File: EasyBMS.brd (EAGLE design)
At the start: 100 x 100 mm, 147 parts, among them Q1 BSS84LT1G, Q10 BSS84LT1G, Q11 BSS84LT1G, Q12 BSS84LT1G, Q14 BSS84LT1G, Q3 BSS84LT1G, Q4 BSS84LT1G, Q5 BSS84LT1G, Q6 BSS84LT1G, Q7 BSS84LT1G, Q8 BSS84LT1G, Q9 BSS84LT1G

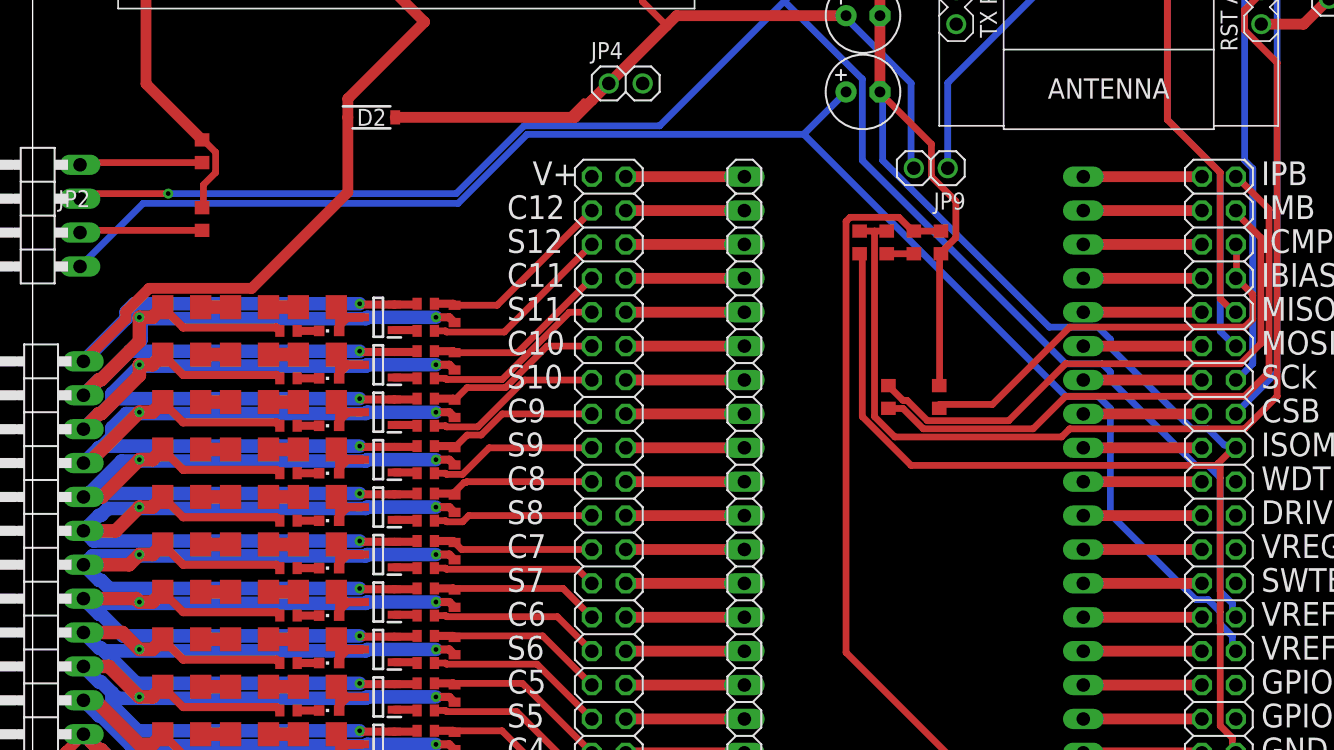
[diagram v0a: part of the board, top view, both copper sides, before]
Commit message: supply voltage bug removed
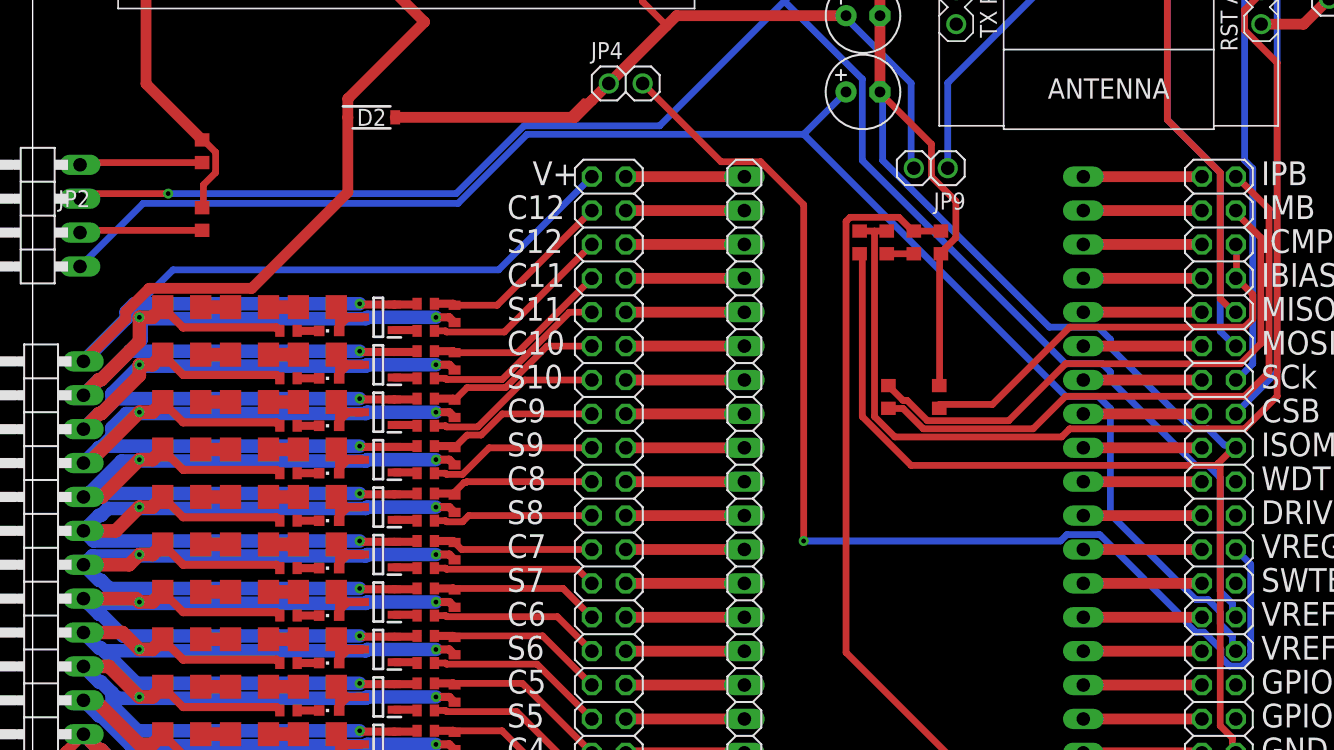
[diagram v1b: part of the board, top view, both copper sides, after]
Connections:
- removed net N$106: JP4.2
- removed net V+: JP5.1
- net P13: now also JP5.1
- net VREG: now also JP4.2
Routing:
- net VREG: track 0.00 -> 88.1 mm, vias 0 -> 1
- net P13: track 122.6 -> 166.5 mm
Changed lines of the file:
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@@
 <wire x1="89.916" y1="28.0416" x2="90.17" y2="27.94" width="0.508" layer="16"/>
-</signal>
-<signal name="N$106">
-<contactref element="JP4" pad="2"/>
 </signal>
 <signal name="MOSI">
@@
 <wire x1="23.625" y1="65.405" x2="23.625" y2="59.7902" width="0.8128" layer="1"/>
 <wire x1="23.625" y1="59.7902" x2="16.4253" y2="52.5905" width="0.8128" layer="1"/>
+<contactref element="JP5" pad="1"/>
+<wire x1="3.81" y1="47.117" x2="7.2672" y2="50.5742" width="0.508" layer="16"/>
+<wire x1="7.2672" y1="50.5742" x2="7.2672" y2="50.72295" width="0.508" layer="16"/>
+<wire x1="7.2672" y1="50.72295" x2="10.51925" y2="53.975" width="0.508" layer="16"/>
+<wire x1="34.925" y1="53.975" x2="41.91" y2="60.96" width="0.508" layer="16"/>
+<wire x1="10.51925" y1="53.975" x2="34.925" y2="53.975" width="0.508" layer="16"/>
 </signal>
 <signal name="P12">
@@
 <wire x1="53.34" y1="60.96" x2="44.45" y2="60.96" width="0.8128" layer="1"/>
 </signal>
-<signal name="V+">
-<contactref element="JP5" pad="1"/>
-</signal>
 <signal name="IPB">
 <contactref element="JP6" pad="2"/>
@@
 <signal name="VREG">
 <contactref element="JP6" pad="24"/>
+<contactref element="JP4" pad="2"/>
+<via x="57.785" y="33.655" extent="1-16" drill="0.35"/>
+<wire x1="45.72" y1="67.945" x2="51.5874" y2="62.0776" width="0.508" layer="1"/>
+<wire x1="51.5874" y1="62.0776" x2="54.56493125" y2="62.0776" width="0.508" layer="1"/>
+<wire x1="54.56493125" y1="62.0776" x2="57.785" y2="58.85753125" width="0.508" layer="1"/>
+<wire x1="57.785" y1="58.85753125" x2="57.785" y2="33.655" width="0.508" layer="1"/>
+<wire x1="57.785" y1="33.655" x2="77.03246875" y2="33.655" width="0.508" layer="16"/>
+<wire x1="77.03246875" y1="33.655" x2="77.51506875" y2="34.1376" width="0.508" layer="16"/>
+<wire x1="77.51506875" y1="34.1376" x2="79.96493125" y2="34.1376" width="0.508" layer="16"/>
+<wire x1="86.5124" y1="27.47706875" x2="87.16706875" y2="26.8224" width="0.508" layer="16"/>
+<wire x1="89.0524" y1="24.93706875" x2="89.70706875" y2="24.2824" width="0.508" layer="16"/>
+<wire x1="89.70706875" y1="24.2824" x2="90.63293125" y2="24.2824" width="0.508" layer="16"/>
+<wire x1="90.63293125" y1="24.2824" x2="91.2876" y2="24.93706875" width="0.508" layer="16"/>
+<wire x1="86.5124" y1="27.59013125" x2="86.5124" y2="27.47706875" width="0.508" layer="16"/>
+<wire x1="87.16706875" y1="26.8224" x2="87.78813125" y2="26.8224" width="0.508" layer="16"/>
+<wire x1="87.78813125" y1="26.8224" x2="89.0524" y2="25.55813125" width="0.508" layer="16"/>
+<wire x1="89.0524" y1="25.55813125" x2="89.0524" y2="24.93706875" width="0.508" layer="16"/>
+<wire x1="79.96493125" y1="34.1376" x2="86.5124" y2="27.59013125" width="0.508" layer="16"/>
+<wire x1="91.2876" y1="24.93706875" x2="91.2876" y2="25.4" width="0.508" layer="16"/>
+<wire x1="91.2876" y1="25.4" x2="91.2876" y2="25.8826" width="0.508" layer="16"/>
+<wire x1="90.17" y1="33.02" x2="91.2876" y2="31.9024" width="0.508" layer="16"/>
+<wire x1="91.2876" y1="25.8826" x2="91.2876" y2="31.9024" width="0.508" layer="16"/>
 </signal>
 <signal name="SWTEN">

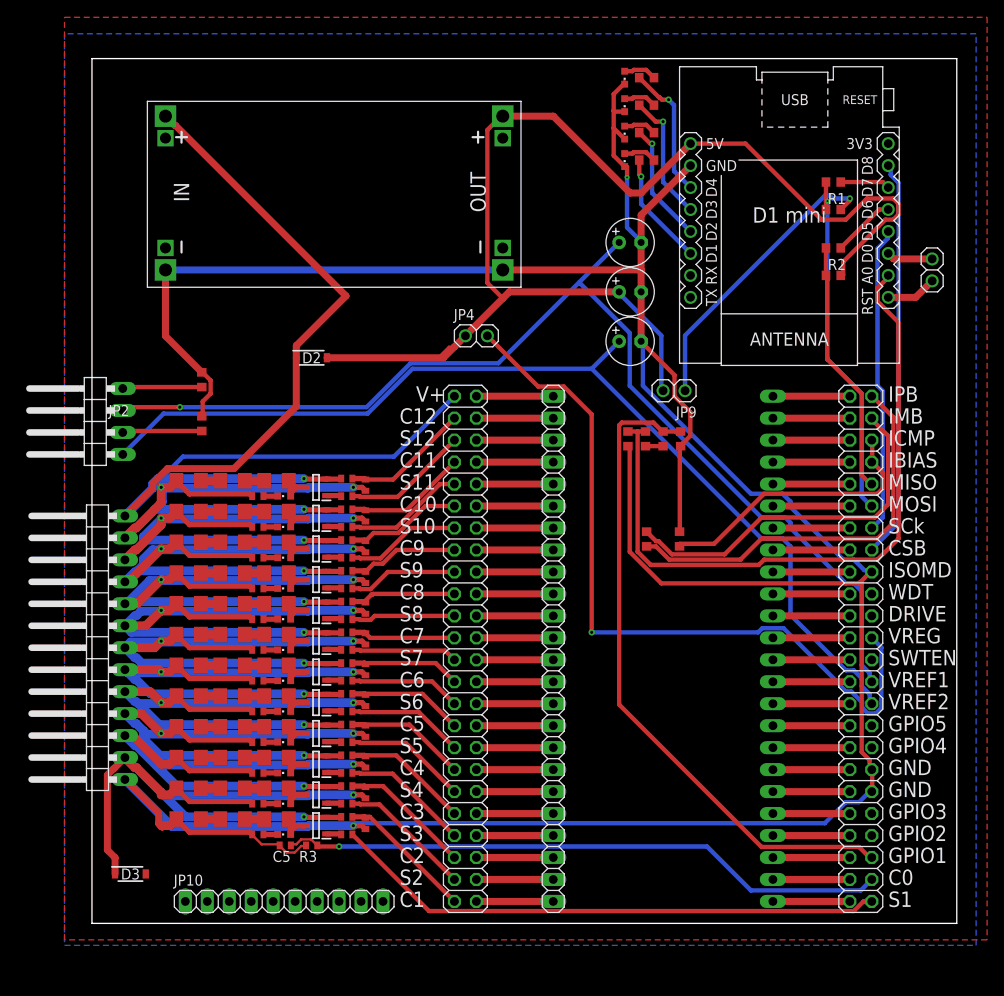
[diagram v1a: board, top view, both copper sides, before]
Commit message: minimize board size to 100x32
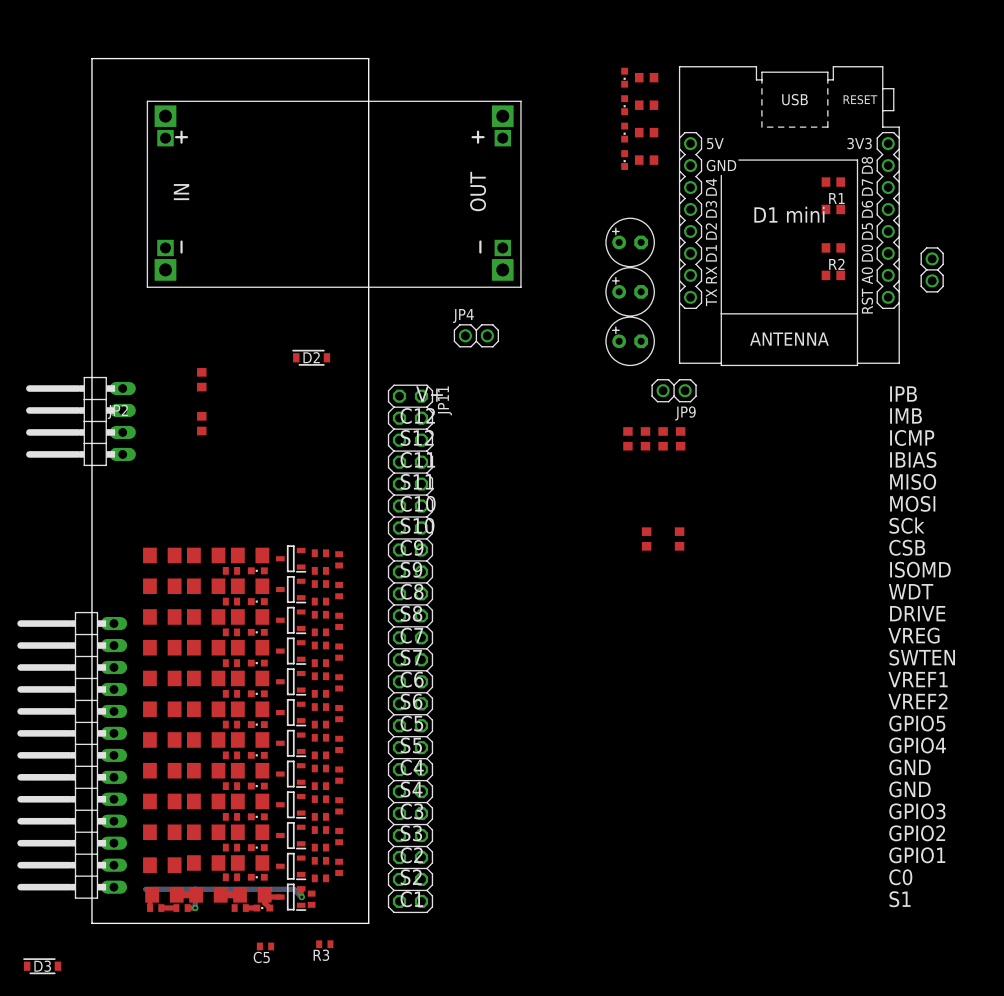
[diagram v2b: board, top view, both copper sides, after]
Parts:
- removed JP10: (no value), pinhead:1X10
- removed JP5, JP6: (no value), pinhead:2X24
- removed JP7, JP8: (no value), pinhead:1X24
- added JP11: (no value), pinhead_own:2X24
- moved C4 26.2 mm to (7.37, 1.78), turned to 180 degrees
- moved R19 21.8 mm to (10.4, 1.78), turned to 0 degrees
- moved D3 14.7 mm to (-5.71, -4.95)
- moved JP1 12.5 mm to (-1.27, 19.4)
- moved C5 11.9 mm to (20.1, -2.67)
- moved R3 11.5 mm to (26.9, -2.41)
- moved R12 9.40 mm to (8.13, 6.73)
- moved R17 9.20 mm to (8.38, 3.30)
- moved R18 9.20 mm to (13.5, 3.30)
- moved R9 9.20 mm to (18.5, 3.30)
- moved C14 9.16 mm to (28.6, 42.0)
- moved C15 9.16 mm to (28.6, 31.4)
- moved C17 9.16 mm to (28.6, 34.9)
- moved LED12 9.16 mm to (19.2, 23.0)
- moved LED13 9.16 mm to (19.2, 37.2)
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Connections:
- removed net N$10: JP5.42, JP7.21
- removed net N$100: JP6.31, JP8.16
- removed net N$101: JP6.29, JP8.15
- removed net N$102: JP6.27, JP8.14
- removed net N$103: JP6.25, JP8.13
- removed net N$104: JP6.23, JP8.12
- removed net N$105: JP6.21, JP8.11
- removed net N$107: JP6.19, JP8.10
- removed net N$108: JP6.17, JP8.9
- removed net N$109: JP6.15, JP8.8
- removed net N$11: JP5.40, JP7.20
- removed net N$110: JP6.13, JP8.7
- removed net N$111: JP6.11, JP8.6
- removed net N$112: JP6.9, JP8.5
- removed net N$113: JP6.7, JP8.4
- removed net N$114: JP6.5, JP8.3
- removed net N$115: JP6.3, JP8.2
- removed net N$116: JP6.1, JP8.1
- removed net N$118: JP5.2, JP7.1
- removed net N$12: JP5.38, JP7.19
- removed net N$13: JP5.36, JP7.18
- removed net N$21: JP5.34, JP7.17
- removed net N$24: JP5.32, JP7.16
- removed net N$61: JP5.30, JP7.15
- removed net N$74: JP5.28, JP7.14
- removed net N$75: JP5.26, JP7.13
- removed net N$76: JP5.24, JP7.12
- removed net N$77: JP5.22, JP7.11
- removed net N$78: JP5.20, JP7.10
- removed net N$8: JP5.46, JP7.23
- removed net N$84: JP5.18, JP7.9
- removed net N$85: JP5.16, JP7.8
- removed net N$86: JP5.14, JP7.7
- removed net N$87: JP5.12, JP7.6
- removed net N$88: JP5.10, JP7.5
- removed net N$89: JP5.8, JP7.4
- removed net N$9: JP5.44, JP7.22
- removed net N$90: JP5.6, JP7.3
- removed net N$91: JP5.4, JP7.2
- removed net N$92: JP6.47, JP8.24
- removed net N$93: JP6.45, JP8.23
- removed net N$94: JP6.43, JP8.22
- removed net N$95: JP6.41, JP8.21
- removed net N$96: JP6.39, JP8.20
- removed net N$97: JP6.37, JP8.19
- removed net N$98: JP6.35, JP8.18
- removed net N$99: JP6.33, JP8.17
- new net C: C4.1, R19.1
- new net LOWER: C4.2, R17.1, R82.2
- new net S: R13.1
- new net UPPERCELL: Q1.2, R19.2
- net C0: now also JP11.46; no longer JP6.46
- net C1: now also JP11.47; no longer C4.1, JP5.47, R19.1
- net C10: now also JP11.11; no longer JP5.11
- net C11: now also JP11.7; no longer JP5.7
- net C12: now also JP11.3; no longer JP5.3
- net C2: now also JP11.43; no longer JP5.43
- net C3: now also JP11.39; no longer JP5.39
- net C4: now also JP11.35; no longer JP5.35
- net C5: now also JP11.31; no longer JP5.31
- net C6: now also JP11.27; no longer JP5.27
- net C7: now also JP11.23; no longer JP5.23
- net C8: now also JP11.19; no longer JP5.19
- net C9: now also JP11.15; no longer JP5.15
- net CSB: now also JP11.16; no longer JP6.16
- net DRIVE: now also JP11.22; no longer JP6.22
- net GND: now also JP11.18, JP11.36, JP11.38; no longer C4.2, C5.2, D3.2, JP10.1, JP10.10, JP10.2, JP10.3, JP10.4, JP10.5, JP10.6, JP10.7, JP10.8, JP10.9, JP6.18, JP6.36, JP6.38, R17.1, R3.2, R82.2
- net GPIO1: now also JP11.44; no longer JP6.44
- net GPIO2: now also JP11.42; no longer JP6.42
- net GPIO3: now also JP11.40; no longer JP6.40
- net GPIO4: now also JP11.34; no longer JP6.34
- net GPIO5: now also JP11.32; no longer JP6.32
- net ICMP: now also JP11.6, JP11.8; no longer JP6.6, JP6.8
- net IMB: now also JP11.4; no longer JP6.4
- net IPB: now also JP11.2; no longer JP6.2
- net MISO: now also JP11.10; no longer JP6.10
- net MOSI: now also JP11.12; no longer JP6.12
- net N$7: now also R3.2; no longer JP5.48, JP7.24
- net P13: now also JP11.1; no longer JP5.1
- net P2: no longer D3.1, Q1.2, R19.2
- net S1: now also JP11.48; no longer JP6.48, R13.1
- net S10: now also JP11.13; no longer JP5.13
- net S11: now also JP11.9; no longer JP5.9
- net S12: now also JP11.5; no longer JP5.5
- net S2: now also JP11.45; no longer JP5.45
- net S3: now also JP11.41; no longer JP5.41
- net S4: now also JP11.37; no longer JP5.37
- net S5: now also JP11.33; no longer JP5.33
- net S6: now also JP11.29; no longer JP5.29
- net S7: now also JP11.25; no longer JP5.25
- net S8: now also JP11.21; no longer JP5.21
- net S9: now also JP11.17; no longer JP5.17
- net SCK: now also JP11.14; no longer JP6.14
- net SWTEN: now also JP11.26; no longer JP6.26
- net VREF1: now also JP11.28; no longer JP6.28
- net VREF2: now also JP11.30; no longer JP6.30
- net VREG: now also JP11.24; no longer JP6.24
- net WDT: now also JP11.20; no longer JP6.20
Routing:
- net GND: track 379.7 -> 0.00 mm, vias 2 -> 0
- net P13: track 166.5 -> 0.00 mm, vias 1 -> 0
- net 5VDC: track 156.8 -> 0.00 mm
- net VREF1: track 127.9 -> 0.00 mm, vias 1 -> 0
- net VREF2: track 117.0 -> 0.00 mm
- net P10: track 93.1 -> 0.00 mm, vias 3 -> 0
- net P9: track 92.9 -> 0.00 mm, vias 3 -> 0
- net P8: track 92.8 -> 0.00 mm, vias 3 -> 0
- net P6: track 92.5 -> 0.00 mm, vias 3 -> 0
- net P7: track 92.4 -> 0.00 mm, vias 3 -> 0
- net P5: track 91.6 -> 0.00 mm, vias 3 -> 0
- net VREG: track 88.1 -> 0.00 mm, vias 1 -> 0
- net P2: track 83.7 -> 0.00 mm, vias 2 -> 0
- net A0IN: track 80.0 -> 0.00 mm
- net GPIO1: track 76.5 -> 0.00 mm
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- removed copper zone on layer 1, net GND
- removed copper zone on layer 16, net GND
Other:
- board size 100 x 100 mm -> 32 x 100 mm
